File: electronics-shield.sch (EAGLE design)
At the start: 92 parts, among them IC1 TLE9201SG, IC2 TLE9201SG, IC3 TLE9201SG, IC4 TLE9201SG, IC5 AOZ1232QI-01, IC6 AOZ1232QI-01, IC7 DS3231SN#, J1 USB-MICRO-B, Q2 ON-SEMICONDUCTOR---NTZD3154NT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, Q3 ON-SEMICONDUCTOR---NTZD3154NT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, U1 STM32F0XX8T, U2 EEPROM-I2C, X1 CONNECTOR_PHOENIX_3.81, X2 Listwa zaciskowa rozłączalna 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, Y2 8MHz

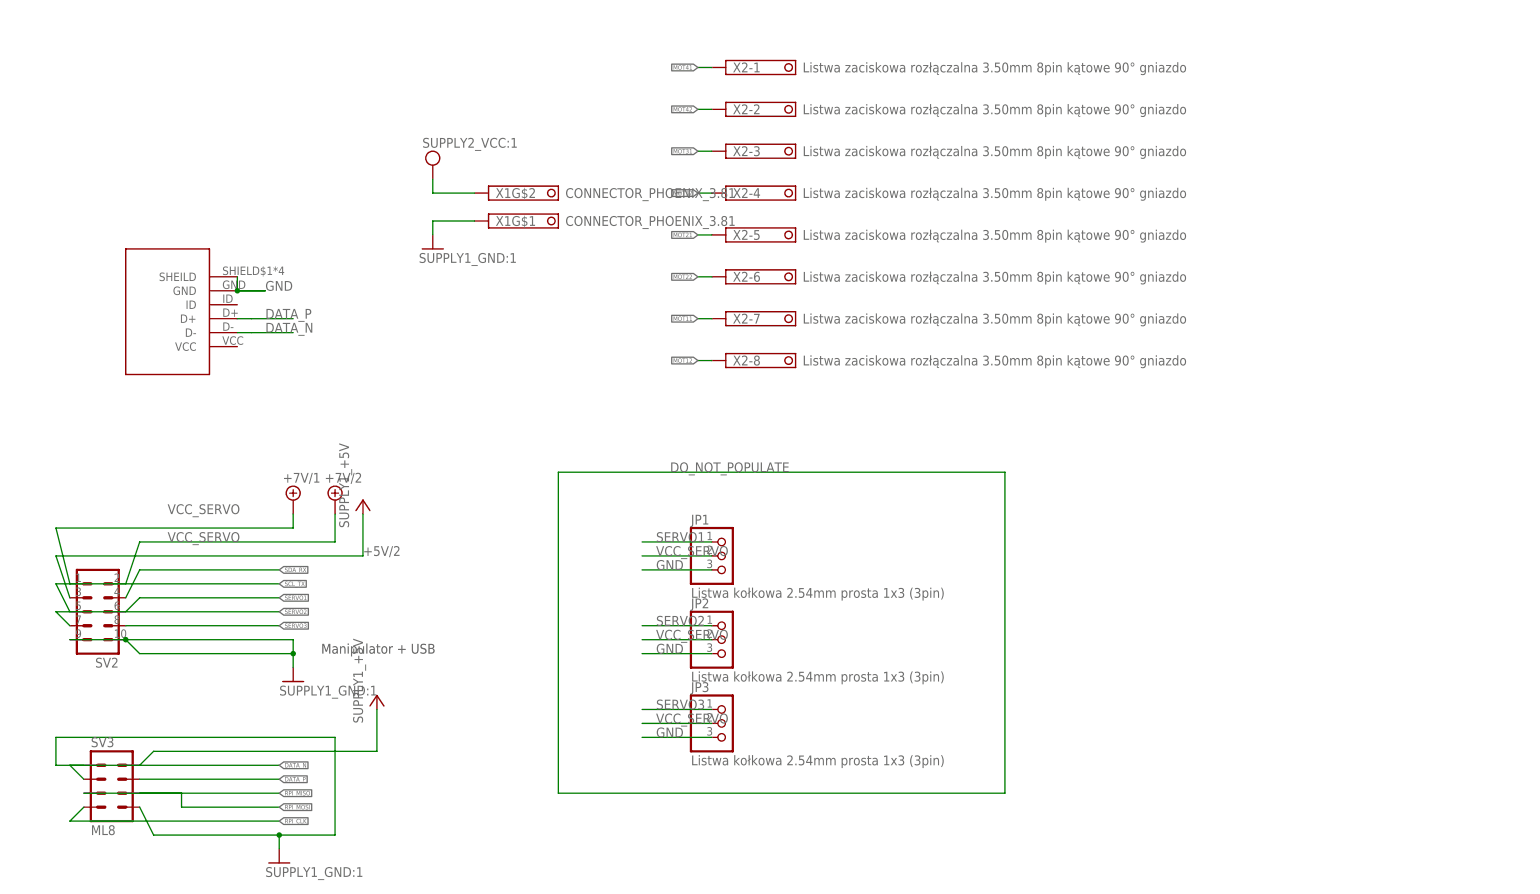
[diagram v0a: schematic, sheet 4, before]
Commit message: Merge branch 'add_RTC' into development
First, basic layout
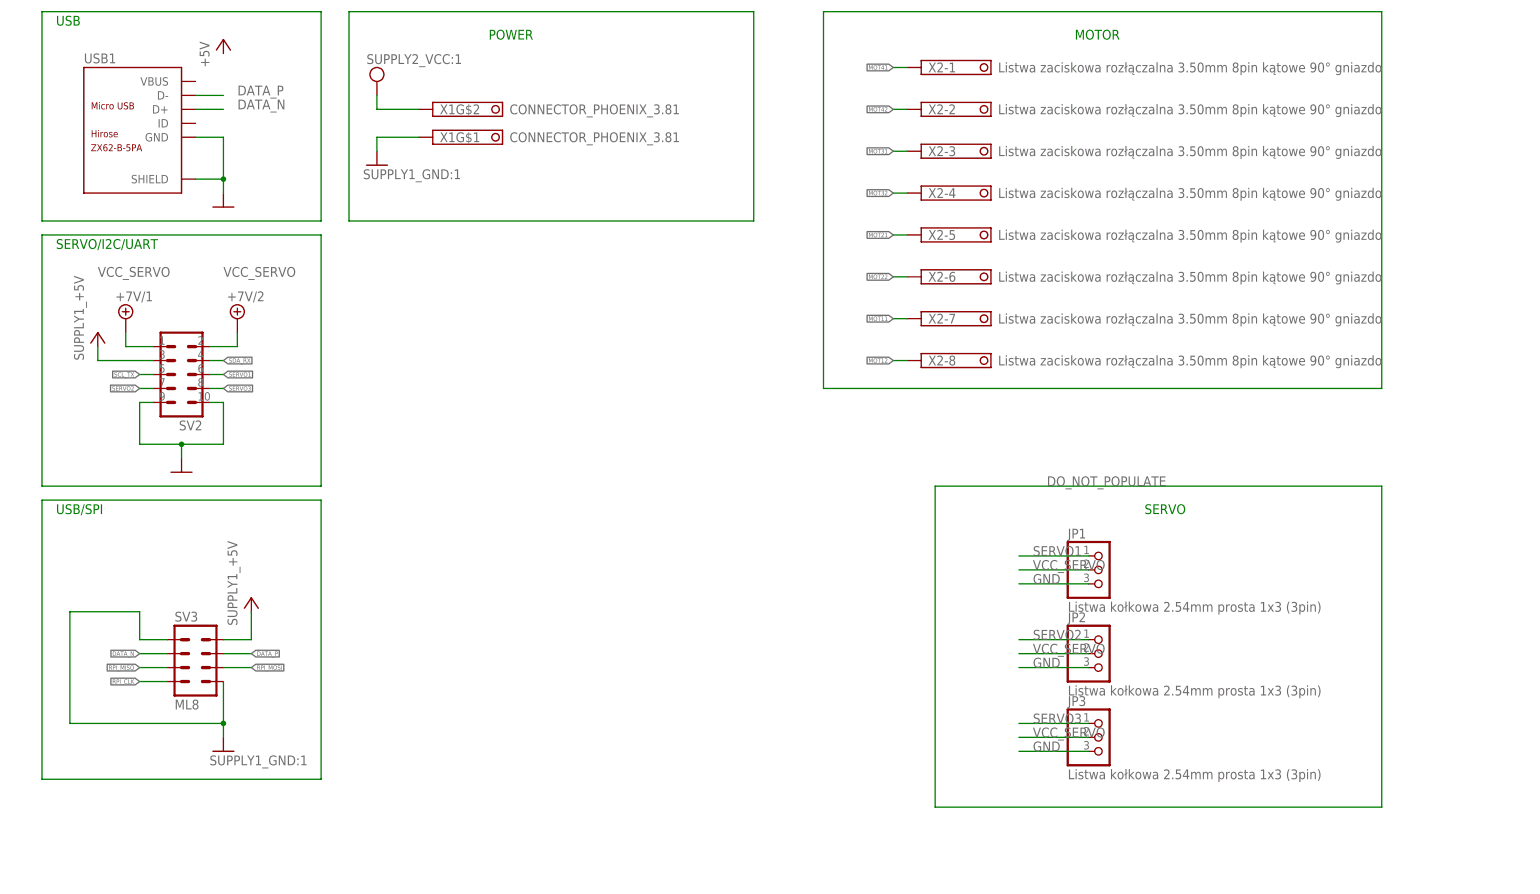
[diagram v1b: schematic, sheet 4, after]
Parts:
- removed J1: USB-MICRO-B, Kell Ideas:USB-MICRO-B
- added USB1: ZX62-B-5PA, Seeed-Connector:MICRO-USB-SMD(ZX62-B-5PA)
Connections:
- net DATA_N: now also USB1.D+; no longer J1.D-
- net DATA_P: now also USB1.D-; no longer J1.D+
- net GND: now also USB1.GND, USB1.SHIELD; no longer J1.GND, J1.SHEILD
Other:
- note added: "MOTOR"
- note added: "POWER"
- note added: "SERVO"
- note added: "SERVO/I2C/UART"
- note added: "USB"
- note added: "USB/SPI"
- note removed: "Manipulator + USB"
- moved on the sheet: JP1, JP2, JP3, SV2, SV3, X1G$1, X1G$2, X2-1, X2-2, X2-3, X2-4, X2-5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

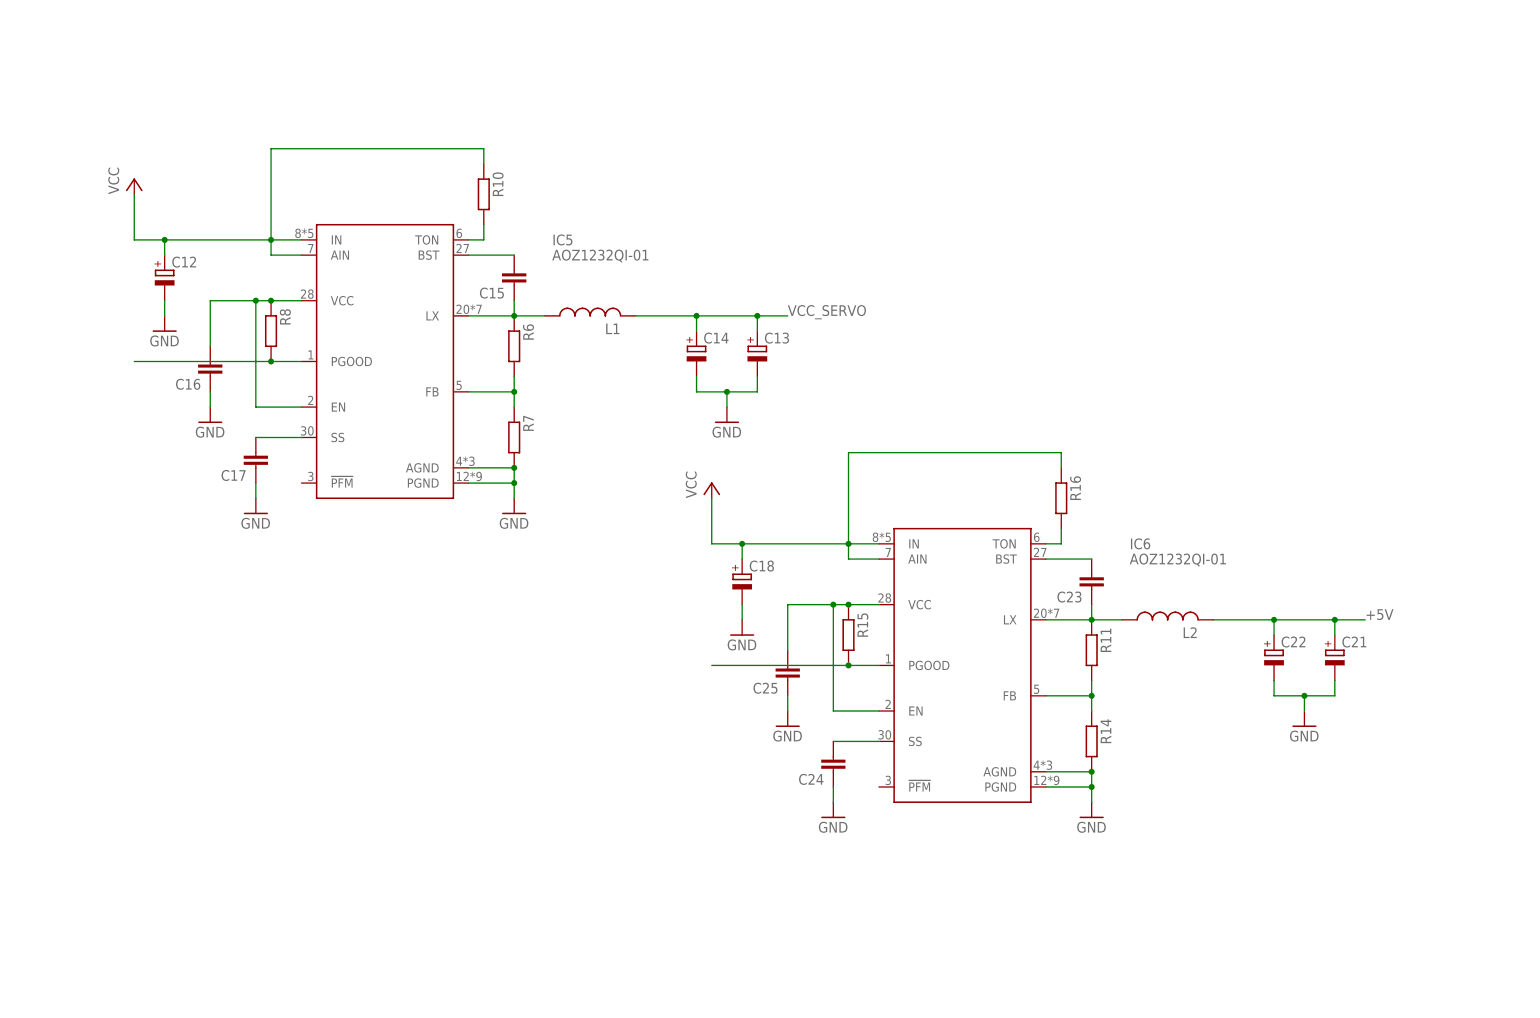
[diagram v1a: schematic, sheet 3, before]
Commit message: Added values for parts in dc-dc converter
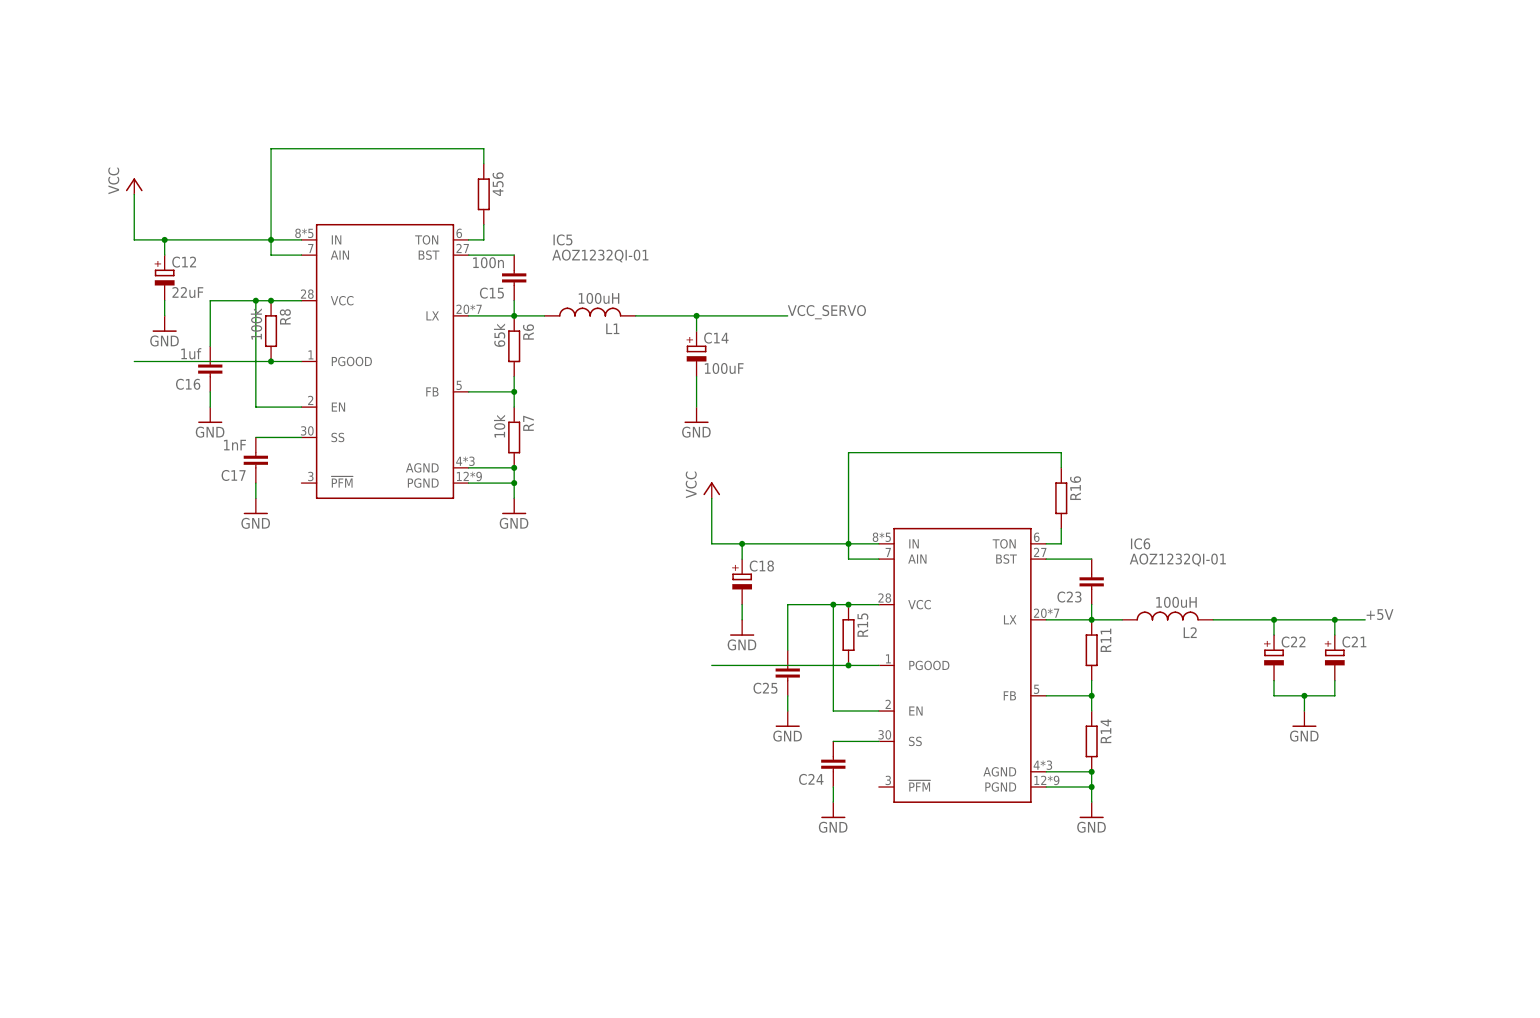
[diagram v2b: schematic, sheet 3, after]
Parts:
- removed C13: (no value), rcl:CPOL-EUB
- C12: value (none) -> 22uF
- C14: value (none) -> 100uF
- C15: value (none) -> 100n
- C16: value (none) -> 1uf
- C17: value (none) -> 1nF
- L1, L2: value (none) -> 100uH
- R6: value (none) -> 65k
- R7: value (none) -> 10k
- R8: value (none) -> 100k
- renumbered R10 to 456
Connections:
- net GND: no longer C13.-
- net VCC_SERVO: no longer C13.+

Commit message: Minor changes, changed RTC, added 3V3 regulator, changed USB connector, added fuses, reverse polarity protection, changed footprint for Schottky diodes, added filtering to input voltage, change in layout
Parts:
- removed 456: (no value), Kell Ideas:RESISTOR_SMD_0603
- removed C19: (no value), Kell Ideas:CAPACITOR_SMD_0603
- removed IC5: AOZ1232QI-01, Kell Ideas:AOZ1232QI-01
- removed IC7: DS3231SN#, Kell Ideas:DS3231SN#
- removed L1: 100uH, rcl:L-USL4532P
- removed Q3: ON-SEMICONDUCTOR---NTZD3154NT1G_ON_SEMICONDUCTOR_NTZD3154NT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, electronics-shield:ON-SEMICONDUCTOR---NTZD3154NT1G_ON_SEMICONDUCTOR_NTZD3154NT1GON_SEMICONDUCTOR_NTZD3154NT1G_0_0
- removed RN1, RN2: 1k, SparkFun-Resistors:1KOHM-ARRAY(4)-0805_ARV-1/10W-5%
- removed USB1: ZX62-B-5PA, Seeed-Connector:MICRO-USB-SMD(ZX62-B-5PA)
- added C13: 47uF, rcl:CPOL-EUC
- added C27, C31, C32: 33uF/10V, rcl:CPOL-EUB
- added C28: 100n, Kell Ideas:CAPACITOR_SMD_0603
- added C29: 1nF, Kell Ideas:CAPACITOR_SMD_0603
- added C30: 1uF/35V, Kell Ideas:CAPACITOR_SMD_0603
- added D17: 10V, diode:ZENER-DIODESOD80C
- added F1, F2, F5: 750mA, Seeed-Fuse:SMD-PPTC-500MA(1206)
- added F3: MF-MSMF050-2, Seeed-Fuse:SMD-PPTC-USE-PPTC-0.50A-15V-0.15OHM(1812)
- added IC8: AOZ1232QI-01, Kell Ideas:AOZ1232QI-01
- added L3: 1uH, rcl:L-USL4532P
- added Q1: (no value), adafruit:MOSFET-NREFLOW
- added R21: 10k, Kell Ideas:RESISTOR_SMD_0603
- added R22: 100k, Kell Ideas:RESISTOR_SMD_0603
- added R23, R24: 456, Kell Ideas:RESISTOR_SMD_0603
- added U3: MAXIM_DS3231MZ+MAXIM_DS3231MZ+_0_0, Kell Ideas:MAXIM_DS3231MZ+MAXIM_DS3231MZ+_0_0
- added U4: V_REG_317SMD, Kell Ideas:V_REG_317SMD
- added X3: C-GRID-04-70553, con-molex:C-GRID-04-70553
- C1, C2, C3, C4: value (none) -> 100nF
- C12: value 22uF -> 47uF; device rcl:CPOL-EUB -> rcl:CPOL-EUC
- C14: value 100uF -> 22uF; device rcl:CPOL-EUB -> Kell Ideas:CAPACITOR_SMD_0603
- C15: value 100n -> 100nF
- C16: value 1uf -> 100nF
- C17: value 1nF -> 22uF
- C18: value (none) -> 22uF/35V
- C21: value (none) -> 33uF/10V
- C22: value (none) -> 100n; device rcl:CPOL-EUB -> Kell Ideas:CAPACITOR_SMD_0603
- C23: value (none) -> 1nF
- C24: value (none) -> 1uF/35V
- C25: value (none) -> 22uF/35V; device Kell Ideas:CAPACITOR_SMD_0603 -> rcl:CPOL-EUB
- D1, D10, D12, D13, D14, D15, D16, D2, D3, D4, D5, D6, D7, D8, D9: value SK38SMA -> 80V/3A; device Kell Ideas:DIODE_SMD -> adafruit:DIODE_SOD-123FL; LINK http://www.tme.eu/pl/details/sk38sma-dio/diody-schottky-smd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 -> (none)
- D11: value SK38SMA -> 80V/3A; device Kell Ideas:DIODE_SMD -> adafruit:DIODE_SOD-123FL; LINK http://www.tme.eu/pl/details/sk38sma-dio/diody-schottky-smd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 -> (none); SPICEPREFIX D -> (none)
- L2: value 100uH -> 1uH
- Q2: value ON-SEMICONDUCTOR---NTZD3154NT1G_ON_SEMICONDUCTOR_NTZD3154NT1GON_SEMICONDUCTOR_NTZD3154NT1G_0_0 -> IRFR5305; device electronics-shield:ON-SEMICONDUCTOR---NTZD3154NT1G_ON_SEMICONDUCTOR_NTZD3154NT1GON_SEMICONDUCTOR_NTZD3154NT1G_0_0 -> transistor-power:IRFR5305
- R11, R16: value (none) -> 65k
- R14: value (none) -> 10k
- R15: value (none) -> 100k
- R6: value 65k -> 10k; device Kell Ideas:RESISTOR_SMD_0603 -> rcl:R-EU_R0603
- R7: device Kell Ideas:RESISTOR_SMD_0603 -> rcl:R-EU_R0603
- R8: value 100k -> 10k; device Kell Ideas:RESISTOR_SMD_0603 -> rcl:R-EU_R0603
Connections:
- removed net +5V/2: SV2.3
- removed net BST: C15.2, IC5.BST
- removed net FB: IC5.FB, R6.2, R7.1
- removed net LX: C15.1, IC5.LX, L1.1, R6.1
- removed net LX1: C23.1, IC6.LX, L2.1, R11.1
- removed net N$14: Q2B.S2, RN2C.1
- removed net N$16: Q2B.D2, RN2D.1
- removed net PGOOD: IC5.PGOOD, R8.2
- removed net SEN1: U1PA.PA0
- removed net SEN2: U1PA.PA1
- removed net SEN3: U1PA.PA2
- removed net SEN4: U1PA.PA3
- removed net SS: C17.2, IC5.SS
- removed net TON: 456.2, IC5.TON
- removed net VCC_INT: C16.2, IC5.EN, IC5.VCC, R8.1
- new net BST2: C28.2, IC8.BST
- new net FB2: IC8.FB, R16.2, R21.1
- new net LX2: C28.1, IC8.LX, L3.1, R16.1
- new net LX3: C22.1, IC6.LX, L2.1, R11.1
- new net N$12: F2.2, SV2.3
- new net N$13: D17.A, Q2.G, R8.2
- new net N$15: F1.1, SV3.P$2
- new net N$17: C15.2, C16.2, F5.2, U4.IN
- new net N$18: F3.1, PCB1.5V0@1, PCB1.5V0@2
- new net PGOOD2: IC8.PGOOD, R22.2
- new net SS2: C29.2, IC8.SS
- new net TON2: IC8.TON, R23.2
- new net UART_SELECTOR: PCB1.GPIO04/GCKL
- new net V+: Q2.D, X1G$2.K
- new net VCC_INT2: C30.2, IC8.EN, IC8.VCC, R22.1
- net +3V3: now also C14.2, C17.2, Q1.G, R6.1, U4.OUT; no longer IC7.VCC, Q2A.G1, Q2B.G2, Q3A.G1, Q3B.G2, RN1A.2, RN1C.2, RN2A.2, RN2C.2
- net +5V: now also C27.+, C31.+, F1.2, F2.1, F3.2, F5.1, L3.2, R7.1; no longer C19.1, C21.+, C22.+, L2.2, PCB1.5V0@1, PCB1.5V0@2, RN1B.2, RN1D.2, RN2B.2, RN2D.2, SV3.P$2
- net BATTERY: no longer IC7.VBAT
- net BST1: now also C22.2; no longer C23.2
- net DATA_N: now also X3-3.S; no longer USB1.D+
- net DATA_P: now also X3-2.S; no longer USB1.D-
- net GND: now also C13.-, C14.1, C15.1, C23.1, C25.-, C27.-, C29.1, C30.1, C31.-, C32.-, IC8.AGND, IC8.PGND, R21.2, R8.1, U4.ADJ, X3-1.S; no longer C14.-, C19.2, C22.-, C25.1, IC5.AGND, IC5.PGND, IC7.!RST, IC7.GND, IC7.NC_1, IC7.NC_2, IC7.NC_3, IC7.NC_4, IC7.NC_5, IC7.NC_6, IC7.NC_7, IC7.NC_8, R7.2, USB1.GND, USB1.SHIELD
- net N$2: no longer IC7.32KHZ
- net N$3: no longer IC7.!INT!/SQW
- net SCL: no longer IC7.SCL
- net SDA: no longer IC7.SDA
- net SERVO1: no longer Q3B.D2, RN1D.1
- net SERVO1_UC: no longer Q3B.S2, RN1C.1
- net SERVO2: now also Q1.D, R7.2; no longer Q3A.D1, RN1B.1
- net SERVO2_UC: now also Q1.S, R6.2; no longer Q3A.S1, RN1A.1
- net SERVO3: no longer Q2A.D1, RN2B.1
- net SERVO3_UC: no longer Q2A.S1, RN2A.1
- net SS1: now also C23.2; no longer C24.2
- net TON1: now also R24.2; no longer R16.2
- net VCC: now also C13.+, C25.+, D17.C, IC8.AIN, IC8.IN, Q2.S, R23.1, R24.1; no longer 456.1, IC5.AIN, IC5.IN, R16.1, X1G$2.K
- net VCC_INT1: now also C24.2; no longer C25.2
- net VCC_SERVO: now also C21.+, C32.+, L2.2; no longer C14.+, L1.2
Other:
- note added: "DO NOT CONNECT"

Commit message: Removed unnecessary stuff, cleaning
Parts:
- removed BT1: 6.8MM_COIN_CELL, SparkFun-Batteries:BATTERY-6.8MM_SMD
- removed C18, C25: 22uF/35V, rcl:CPOL-EUB
- removed C20, C26: (no value), Kell Ideas:CAPACITOR_SMD_0603
- removed C21, C27, C31, C32: 33uF/10V, rcl:CPOL-EUB
- removed C22, C28: 100n, Kell Ideas:CAPACITOR_SMD_0603
- removed C23, C29: 1nF, Kell Ideas:CAPACITOR_SMD_0603
- removed C24, C30: 1uF/35V, Kell Ideas:CAPACITOR_SMD_0603
- removed IC6, IC8: AOZ1232QI-01, Kell Ideas:AOZ1232QI-01
- removed L2, L3: 1uH, rcl:L-USL4532P
- removed R11, R16: 65k, Kell Ideas:RESISTOR_SMD_0603
- removed R14, R21: 10k, Kell Ideas:RESISTOR_SMD_0603
- removed R15, R22: 100k, Kell Ideas:RESISTOR_SMD_0603
- removed R17, R18, R19, R20: (no value), Kell Ideas:RESISTOR_SMD_0603
- removed R23, R24: 456, Kell Ideas:RESISTOR_SMD_0603
- removed U2: EEPROM-I2C, Kell Ideas:EEPROM-I2C
- removed U3: MAXIM_DS3231MZ+MAXIM_DS3231MZ+_0_0, Kell Ideas:MAXIM_DS3231MZ+MAXIM_DS3231MZ+_0_0
- removed X3: C-GRID-04-70553, con-molex:C-GRID-04-70553
- added U$1, U$2: POLOLU_D24V22FX, Kell Ideas:POLOLU_D24V22FX
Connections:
- net UART_SELECTOR renamed SIGNAL_SELECTOR
- removed net BATTERY: BT1.+
- removed net BST1: C22.2, IC6.BST
- removed net BST2: C28.2, IC8.BST
- removed net FB1: IC6.FB, R11.2, R14.1
- removed net FB2: IC8.FB, R16.2, R21.1
- removed net LX2: C28.1, IC8.LX, L3.1, R16.1
- removed net LX3: C22.1, IC6.LX, L2.1, R11.1
- removed net N$2: R18.1
- removed net N$3: R17.1
- removed net PGOOD1: IC6.PGOOD, R15.2
- removed net PGOOD2: IC8.PGOOD, R22.2
- removed net SS1: C23.2, IC6.SS
- removed net SS2: C29.2, IC8.SS
- removed net TON1: IC6.TON, R24.2
- removed net TON2: IC8.TON, R23.2
- removed net VCC_INT1: C24.2, IC6.EN, IC6.VCC, R15.1
- removed net VCC_INT2: C30.2, IC8.EN, IC8.VCC, R22.1
- new net STM_RX: U1PB.PB7
- new net STM_TX: U1PB.PB6
- net +3V3: no longer C20.1, C26.2, R17.2, R18.2, R19.1, R20.1, U2.VCC, U2.WP
- net +5V: now also U$2.VOUT; no longer C27.+, C31.+, L3.2
- net DATA_N: no longer X3-3.S
- net DATA_P: no longer X3-2.S
- net GND: now also U$1.GND, U$2.GND; no longer BT1.-, C18.-, C20.2, C21.-, C23.1, C24.1, C25.-, C26.1, C27.-, C29.1, C30.1, C31.-, C32.-, IC6.AGND, IC6.PGND, IC8.AGND, IC8.PGND, R14.2, R21.2, U2.A1, U2.A2, U2.VSS, X3-1.S
- net RPI_RXD: no longer U1PB.PB6
- net RPI_TXD: no longer U1PB.PB7
- net SCL: no longer R19.2, U1PA.PF6, U2.SCL
- net SDA: no longer R20.2, U1PA.PF7, U2.SDA
- net VCC: now also U$1.VIN, U$2.VIN; no longer C18.+, C25.+, IC6.AIN, IC6.IN, IC8.AIN, IC8.IN, R23.1, R24.1
- net VCC_SERVO: now also U$1.VOUT; no longer C21.+, C32.+, L2.2
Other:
- note removed: "DO NOT CONNECT"
- note removed: "NC"
- note removed: "USB"
